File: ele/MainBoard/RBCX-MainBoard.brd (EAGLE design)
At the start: 100 x 100 mm, 263 parts, among them IC1 DRV8833PWP, IC10 INA180A4, IC2 INA180A4, IC3 INA180A4, IC4 DRV8833PWP, IC5 INA180A4, IC6 INA180A4, IC7 INA180A4, IC8 INA180A4, IC9 INA180A4, Q1 CHOOSE_ME, Q3 CHOOSE_ME, Q6 CHOOSE_ME, Q8 CHOOSE_ME, Q9 CHOOSE_ME, U1 STM32F103VCT6, X0 POWER_IN, X1 M3B, X2 M4B, X3 M3B, X4 M4B, X5 POWER_OUT, Y1 3215_2P, Y2 5032/2P

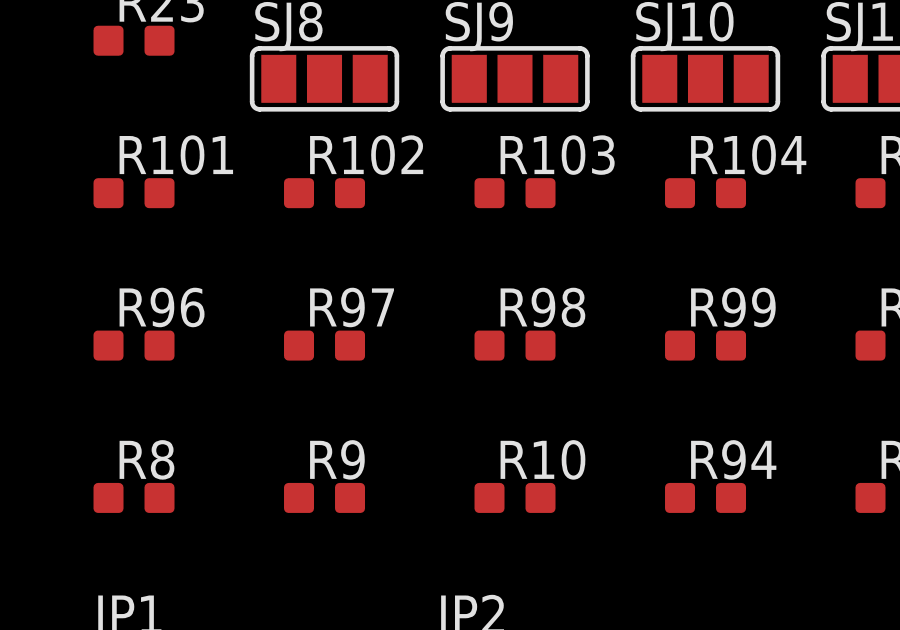
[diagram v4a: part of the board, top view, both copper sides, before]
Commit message: MainBoardSCH: Continue with ESP pinout
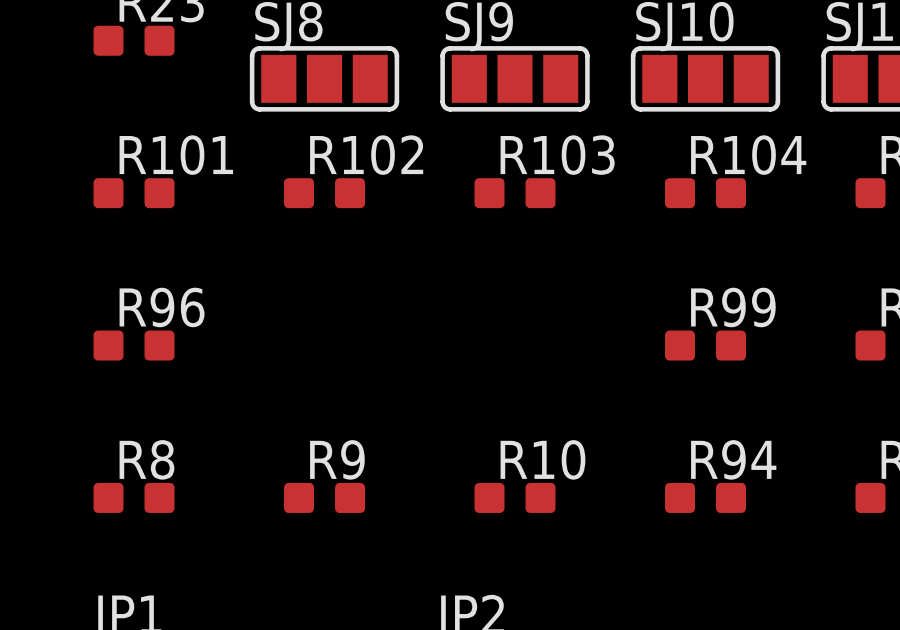
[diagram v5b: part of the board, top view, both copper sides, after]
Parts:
- removed R97, R98: 180R, rcl_upravena:R0603
- JP1: value STM_CAN -> ESP-I2C-CAN-UART
- JP2: value STM_I2C -> ESP_I2C
- JP3: value STM_USART -> ESP_USART
- JP5: value STM_SPI -> ESP_SPI
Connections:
- removed net STM-SPI_MOSI: JP34.3, JP5.3, R86.2, R99.2
- new net ESP-I2C-SCL: JP2.3, R10.2, R22.1
- new net ESP-I2C-SCL-CAN-UART-RX: JP1.3, R7.2
- new net ESP-I2C-SDA: JP2.4, R23.1, R9.2
- new net ESP-I2C-SDA-CAN-UART-TX: JP1.4, R8.2
- new net ESP-SPI-!CS: JP5.6, R102.2
- new net ESP-SPI-MISO: JP5.4, R100.2
- new net ESP-SPI-MOSI: JP5.3, R99.2
- new net ESP-SPI-SCK: JP5.5, R101.2
- new net ESP-USART-DIR: JP3.5, R96.2
- new net ESP-USART-RX: JP3.3, R94.2
- new net ESP-USART-TX: JP3.4, R95.2
- new net ESP_I2C_PWR: JP2.1, R22.2, R23.2, SJ8.2
- new net ESP_USART_PWR: JP3.1, SJ9.2
- new net ESP_USART_PWR1: JP5.1, SJ10.2
- new net N$10: R94.1
- new net N$12: R95.1
- new net N$7: SJ10.1
- new net N$8: SJ9.3
- new net N$9: SJ9.1
- new net STM-SPI-MOSI: JP34.3, R86.2
- net +3V3S: no longer SJ10.1, SJ8.1, SJ9.1
- net +5V0S: no longer JP1.1, SJ10.3, SJ8.3, SJ9.3
- net GND: now also JP1.2, JP2.2, JP3.2, JP5.2
- net I2C_SCL: now also R9.1
- net I2C_SDA: now also R10.1
- net N$2: now also JP1.1; no longer JP3.2
- net N$3: now also SJ8.3; no longer JP5.2
- net N$4: now also SJ8.1; no longer JP2.1
- net N$5: now also SJ10.3; no longer JP1.4
- net SPI_MISO: now also R100.1
- net SPI_MOSI: now also R99.1
- net SPI_SCK: now also R101.1, R102.1
- net STM-CAN-RX: no longer JP1.3, R8.2
- net STM-CAN-TX: no longer JP1.2, R7.2
- net STM-I2C-SCL: no longer JP2.3, R10.2, R22.1
- net STM-I2C-SDA: no longer JP2.4, R23.1, R9.2
- net STM-SPI-!CS: no longer JP5.6, R102.2
- net STM-SPI-MISO: no longer JP5.4, R100.2
- net STM-SPI-SCK: no longer JP5.5, R101.2
- net STM-USART-CK: no longer JP3.7, R98.2
- net STM-USART-CTS: no longer JP3.5, R96.2
- net STM-USART-RTS: no longer JP3.6, R97.2
- net STM-USART-RX: no longer JP3.3, R94.2
- net STM-USART-TX: no longer JP3.4, R95.2
- net STM_I2C_PWR: no longer JP2.2, R22.2, R23.2, SJ8.2
- net STM_USART_PWR: no longer JP3.1, SJ9.2
- net STM_USART_PWR1: no longer JP5.1, SJ10.2

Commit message: MainBoardSCH: Add diode in SOD-123 (B5819W) and replace some +5V0S with +5V
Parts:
- removed D6: SS34, diode:DO214BA
- added D3, U$1: B5819W, SOD-123:SOD-123
- D15: value SS34 -> B5819W; device diode:DO214BA -> SOD-123:SOD-123
- moved D15 590.7 mm to (-135.9, -1347.5)
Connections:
- removed net N$3: SJ8.3
- removed net N$4: SJ8.1
- removed net N$5: SJ10.3
- removed net N$7: SJ10.1
- removed net N$8: SJ9.3
- removed net N$9: SJ9.1
- net +3V3: now also SJ10.1, SJ8.1, SJ9.1
- net +5V: now also JP13.1, JP14.1, JP24.1, JP4.1, JP9.1, SJ10.3, SJ3.3, SJ4.3, SJ5.3, SJ6.3, SJ8.3, SJ9.3
- net +5V0S: no longer JP13.1, JP14.1, JP24.1, JP4.1, JP9.1, SJ3.3, SJ4.3, SJ5.3, SJ6.3
- net ENC34PWR: now also D3.C; no longer D6.C
- net ENC34_PWR: now also D3.A; no longer D6.A

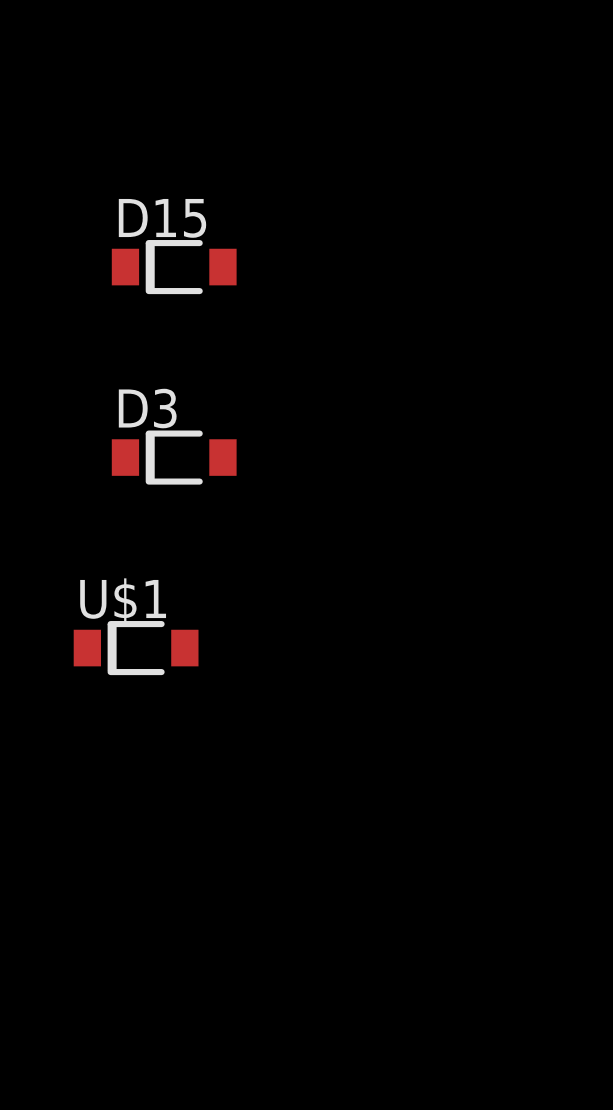
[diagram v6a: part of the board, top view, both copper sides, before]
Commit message: MainBoardSCH: Replace diode in SOD-123 with standard part from eagle_libraries
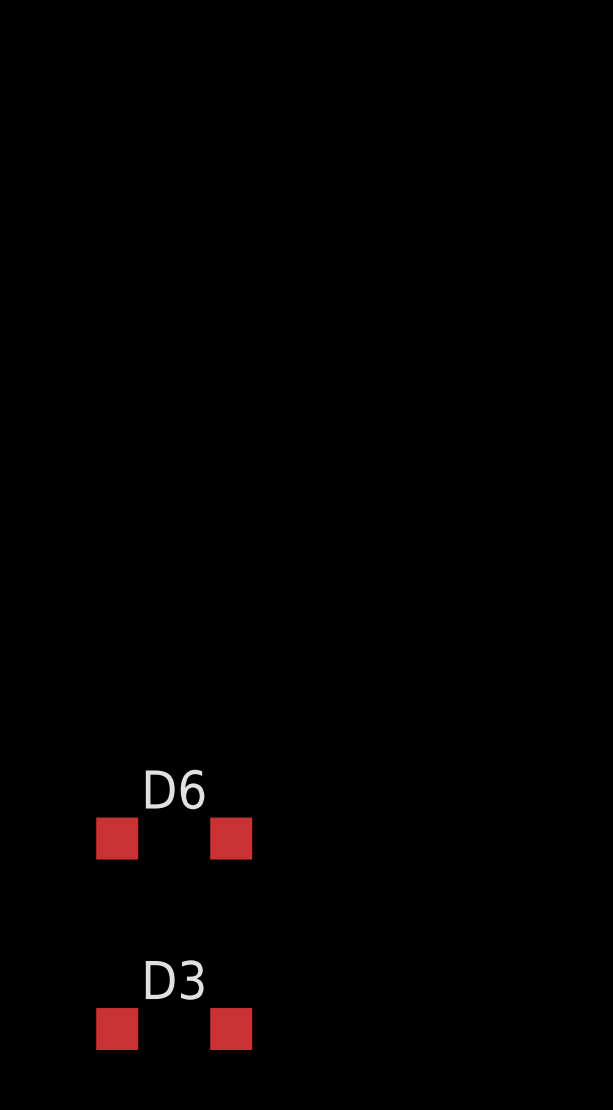
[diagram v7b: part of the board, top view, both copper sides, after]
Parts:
- removed D15, U$1: B5819W, SOD-123:SOD-123
- added D6: B5819W, diode:SOD123
- D3: device SOD-123:SOD-123 -> diode:SOD123
- moved D3 19.0 mm to (-135.9, -1372.9)
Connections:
- net ENC12PWR: now also D6.C; no longer D15.C
- net ENC12_PWR: now also D6.A; no longer D15.A
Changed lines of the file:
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@@
 <attribute name="VALUE" x="-118.745" y="311.785" size="1.27" layer="27"/>
 </element>
-<element name="D15" library="SOD-123" package="SOD-123" value="B5819W" x="-135.89" y="-1347.47" smashed="yes">
-<attribute name="DESCRIPTION" value="40V 1A 600mV @ 1A SOD-123 Schottky Barrier Diodes (SBD) RoHS" x="-135.89" y="-1347.47" size="1.778" layer="27" display="off"/>
-<attribute name="EXTENDED" value="NO" x="-135.89" y="-1347.47" size="1.778" layer="27" display="off"/>
-<attribute name="LCSC_ID" value="C305445" x="-135.89" y="-1347.47" size="1.778" layer="27" display="off"/>
-<attribute name="MF" value="Foshan Blue Rocket Elec" x="-135.89" y="-1347.47" size="1.778" layer="27" display="off"/>
-<attribute name="MF_ID" value="B5819W" x="-135.89" y="-1347.47" size="1.778" layer="27" display="off"/>
-<attribute name="NAME" x="-137.89" y="-1346.47" size="1.27" layer="25"/>
-<attribute name="PACKAGE" value="SOD-123" x="-135.89" y="-1347.47" size="1.778" layer="27" display="off"/>
-<attribute name="PADS" value="2" x="-135.89" y="-1347.47" size="1.778" layer="27" display="off"/>
-<attribute name="PRICE_100PLUS" value="$0.0176" x="-135.89" y="-1347.47" size="1.778" layer="27" display="off"/>
-<attribute name="PRICE_1PLUS" value="$0.0342" x="-135.89" y="-1347.47" size="1.778" layer="27" display="off"/>
-<attribute name="VALUE" x="-137.89" y="-1349.97" size="1.27" layer="27"/>
+<element name="D6" library="diode" package="SOD123" value="B5819W" x="-135.89" y="-1366.52" smashed="yes">
+<attribute name="DESCRIPTION" value="40V 1A 600mV @ 1A SOD-123 Schottky Barrier Diodes (SBD) RoHS" x="-135.89" y="-1366.52" size="1.778" layer="27" display="off"/>
+<attribute name="EXTENDED" value="NO" x="-135.89" y="-1366.52" size="1.778" layer="27" display="off"/>
+<attribute name="LCSC_ID" value="C305445" x="-135.89" y="-1366.52" size="1.778" layer="27" display="off"/>
+<attribute name="MF" value="Foshan Blue Rocket Elec" x="-135.89" y="-1366.52" size="1.778" layer="27" display="off"/>
+<attribute name="MF_ID" value="B5819W" x="-135.89" y="-1366.52" size="1.778" layer="27" display="off"/>
+<attribute name="NAME" x="-136.99" y="-1365.52" size="1.27" layer="25"/>
+<attribute name="PACKAGE" value="SOD-123" x="-135.89" y="-1366.52" size="1.778" layer="27" display="off"/>
+<attribute name="PADS" value="2" x="-135.89" y="-1366.52" size="1.778" layer="27" display="off"/>
+<attribute name="PRICE_100PLUS" value="$0.0176" x="-135.89" y="-1366.52" size="1.778" layer="27" display="off"/>
+<attribute name="PRICE_1PLUS" value="$0.0342" x="-135.89" y="-1366.52" size="1.778" layer="27" display="off"/>
+<attribute name="PRICE_DATE" value="17.03.2020" x="-135.89" y="-1366.52" size="1.778" layer="27" display="off"/>
+<attribute name="VALUE" x="-136.99" y="-1368.82" size="1.27" layer="27"/>
 </element>
-<element name="D3" library="SOD-123" package="SOD-123" value="B5819W" x="-135.89" y="-1353.82" smashed="yes">
-<attribute name="DESCRIPTION" value="40V 1A 600mV @ 1A SOD-123 Schottky Barrier Diodes (SBD) RoHS" x="-135.89" y="-1353.82" size="1.778" layer="27" display="off"/>
-<attribute name="EXTENDED" value="NO" x="-135.89" y="-1353.82" size="1.778" layer="27" display="off"/>
-<attribute name="LCSC_ID" value="C305445" x="-135.89" y="-1353.82" size="1.778" layer="27" display="off"/>
-<attribute name="MF" value="Foshan Blue Rocket Elec" x="-135.89" y="-1353.82" size="1.778" layer="27" display="off"/>
-<attribute name="MF_ID" value="B5819W" x="-135.89" y="-1353.82" size="1.778" layer="27" display="off"/>
-<attribute name="NAME" x="-137.89" y="-1352.82" size="1.27" layer="25"/>
-<attribute name="PACKAGE" value="SOD-123" x="-135.89" y="-1353.82" size="1.778" layer="27" display="off"/>
-<attribute name="PADS" value="2" x="-135.89" y="-1353.82" size="1.778" layer="27" display="off"/>
-<attribute name="PRICE_100PLUS" value="$0.0176" x="-135.89" y="-1353.82" size="1.778" layer="27" display="off"/>
-<attribute name="PRICE_1PLUS" value="$0.0342" x="-135.89" y="-1353.82" size="1.778" layer="27" display="off"/>
-<attribute name="VALUE" x="-137.89" y="-1356.32" size="1.27" layer="27"/>
-</element>
-<element name="U$1" library="SOD-123" package="SOD-123" value="B5819W" x="-137.16" y="-1360.17" smashed="yes">
-<attribute name="DESCRIPTION" value="40V 1A 600mV @ 1A SOD-123 Schottky Barrier Diodes (SBD) RoHS" x="-137.16" y="-1360.17" size="1.778" layer="27" display="off"/>
-<attribute name="EXTENDED" value="NO" x="-137.16" y="-1360.17" size="1.778" layer="27" display="off"/>
-<attribute name="LCSC_ID" value="C305445" x="-137.16" y="-1360.17" size="1.778" layer="27" display="off"/>
-<attribute name="MF" value="Foshan Blue Rocket Elec" x="-137.16" y="-1360.17" size="1.778" layer="27" display="off"/>
-<attribute name="MF_ID" value="B5819W" x="-137.16" y="-1360.17" size="1.778" layer="27" display="off"/>
-<attribute name="NAME" x="-139.16" y="-1359.17" size="1.27" layer="25"/>
-<attribute name="PACKAGE" value="SOD-123" x="-137.16" y="-1360.17" size="1.778" layer="27" display="off"/>
-<attribute name="PADS" value="2" x="-137.16" y="-1360.17" size="1.778" layer="27" display="off"/>
-<attribute name="PRICE_100PLUS" value="$0.0176" x="-137.16" y="-1360.17" size="1.778" layer="27" display="off"/>
-<attribute name="PRICE_1PLUS" value="$0.0342" x="-137.16" y="-1360.17" size="1.778" layer="27" display="off"/>
-<attribute name="VALUE" x="-139.16" y="-1362.67" size="1.27" layer="27"/>
+<element name="D3" library="diode" package="SOD123" value="B5819W" x="-135.89" y="-1372.87" smashed="yes">
+<attribute name="DESCRIPTION" value="40V 1A 600mV @ 1A SOD-123 Schottky Barrier Diodes (SBD) RoHS" x="-135.89" y="-1372.87" size="1.778" layer="27" display="off"/>
+<attribute name="EXTENDED" value="NO" x="-135.89" y="-1372.87" size="1.778" layer="27" display="off"/>
+<attribute name="LCSC_ID" value="C305445" x="-135.89" y="-1372.87" size="1.778" layer="27" display="off"/>
+<attribute name="MF" value="Foshan Blue Rocket Elec" x="-135.89" y="-1372.87" size="1.778" layer="27" display="off"/>
+<attribute name="MF_ID" value="B5819W" x="-135.89" y="-1372.87" size="1.778" layer="27" display="off"/>
+<attribute name="NAME" x="-136.99" y="-1371.87" size="1.27" layer="25"/>
+<attribute name="PACKAGE" value="SOD-123" x="-135.89" y="-1372.87" size="1.778" layer="27" display="off"/>
+<attribute name="PADS" value="2" x="-135.89" y="-1372.87" size="1.778" layer="27" display="off"/>
+<attribute name="PRICE_100PLUS" value="$0.0176" x="-135.89" y="-1372.87" size="1.778" layer="27" display="off"/>
+<attribute name="PRICE_1PLUS" value="$0.0342" x="-135.89" y="-1372.87" size="1.778" layer="27" display="off"/>
+<attribute name="PRICE_DATE" value="17.03.2020" x="-135.89" y="-1372.87" size="1.778" layer="27" display="off"/>
+<attribute name="VALUE" x="-136.99" y="-1375.17" size="1.27" layer="27"/>
 </element>
 </elements>
@@
 <contactref element="JP12" pad="2"/>
 <contactref element="D3" pad="C"/>
-<wire x1="-39.37" y1="-325.12" x2="-137.515" y2="-1353.82" width="0" layer="19" extent="1-1"/>
+<wire x1="-39.37" y1="-325.12" x2="-137.79" y2="-1372.87" width="0" layer="19" extent="1-1"/>
 <wire x1="-39.37" y1="-317.5" x2="-39.37" y2="-325.12" width="0" layer="19" extent="1-1"/>
 </signal>
@@
 <contactref element="SJ2" pad="2"/>
 <contactref element="D3" pad="A"/>
-<wire x1="-22.86" y1="-325.12" x2="-134.265" y2="-1353.82" width="0" layer="19" extent="1-1"/>
+<wire x1="-22.86" y1="-325.12" x2="-133.99" y2="-1372.87" width="0" layer="19" extent="1-1"/>
 </signal>
 <signal name="ENC_3A">
@@
 <signal name="ENC12_PWR">
 <contactref element="SJ1" pad="2"/>
-<contactref element="D15" pad="A"/>
-<wire x1="-50.8" y1="-783.59" x2="-134.265" y2="-1347.47" width="0" layer="19" extent="1-1"/>
+<contactref element="D6" pad="A"/>
+<wire x1="-50.8" y1="-783.59" x2="-133.99" y2="-1366.52" width="0" layer="19" extent="1-1"/>
 </signal>
 <signal name="ENC12PWR">
 <contactref element="JP16" pad="2"/>
 <contactref element="JP17" pad="2"/>
-<contactref element="D15" pad="C"/>
-<wire x1="-63.5" y1="-763.27" x2="-137.515" y2="-1347.47" width="0" layer="19" extent="1-1"/>
+<contactref element="D6" pad="C"/>
+<wire x1="-63.5" y1="-763.27" x2="-137.79" y2="-1366.52" width="0" layer="19" extent="1-1"/>
 <wire x1="-44.45" y1="-755.65" x2="-63.5" y2="-763.27" width="0" layer="19" extent="1-1"/>
 </signal>

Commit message: MainBoardSCH: Replace +5V0S power rail with +5V
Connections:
- removed net +5V0S: D10.2, D16.2, D17.2, D18.2, D19.2, D7.2, D8.2, D9.2, SJ1.3, SJ11.3, SJ2.3
- removed net N$2: JP1.1
- removed net N$6: JP7.2
- net +3V3S: now also D10.2, D16.2, D17.2, D18.2, D19.2, D7.2, D8.2, D9.2
- net +5V: now also JP1.1, SJ1.3, SJ11.3, SJ2.3
- net GND: now also JP7.2
